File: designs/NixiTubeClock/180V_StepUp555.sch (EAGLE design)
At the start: 8 parts, among them IC1 LM555D, IC2 IRF740SPBF, T1 BC547

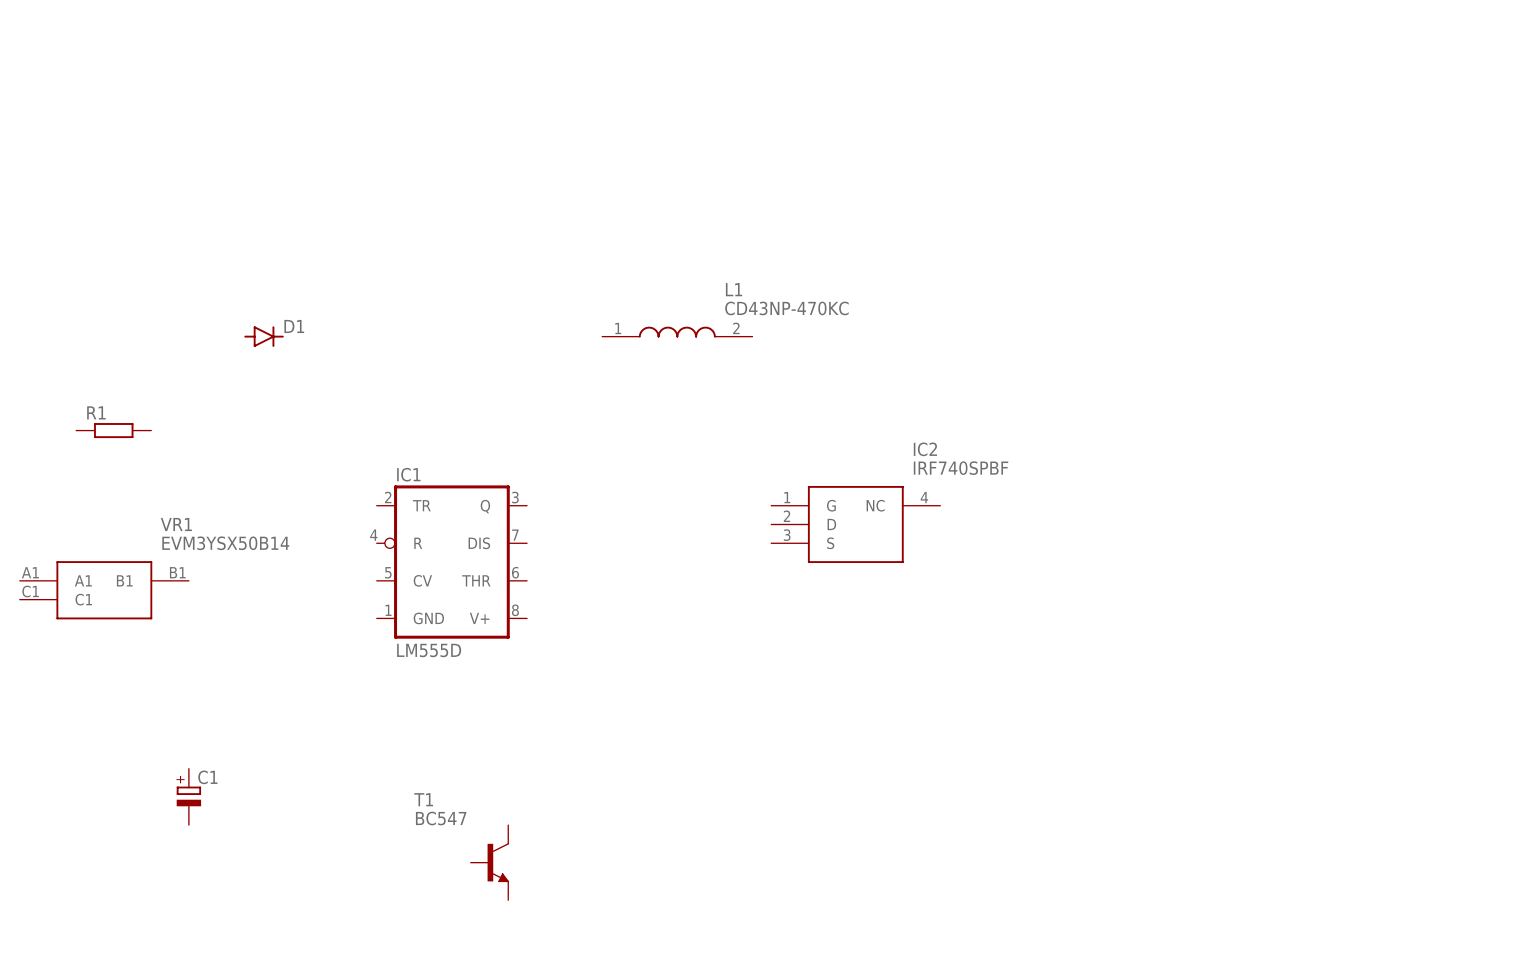
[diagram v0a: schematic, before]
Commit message: added first IN-4 Design and edited mainboard to fit all screws for IN-4
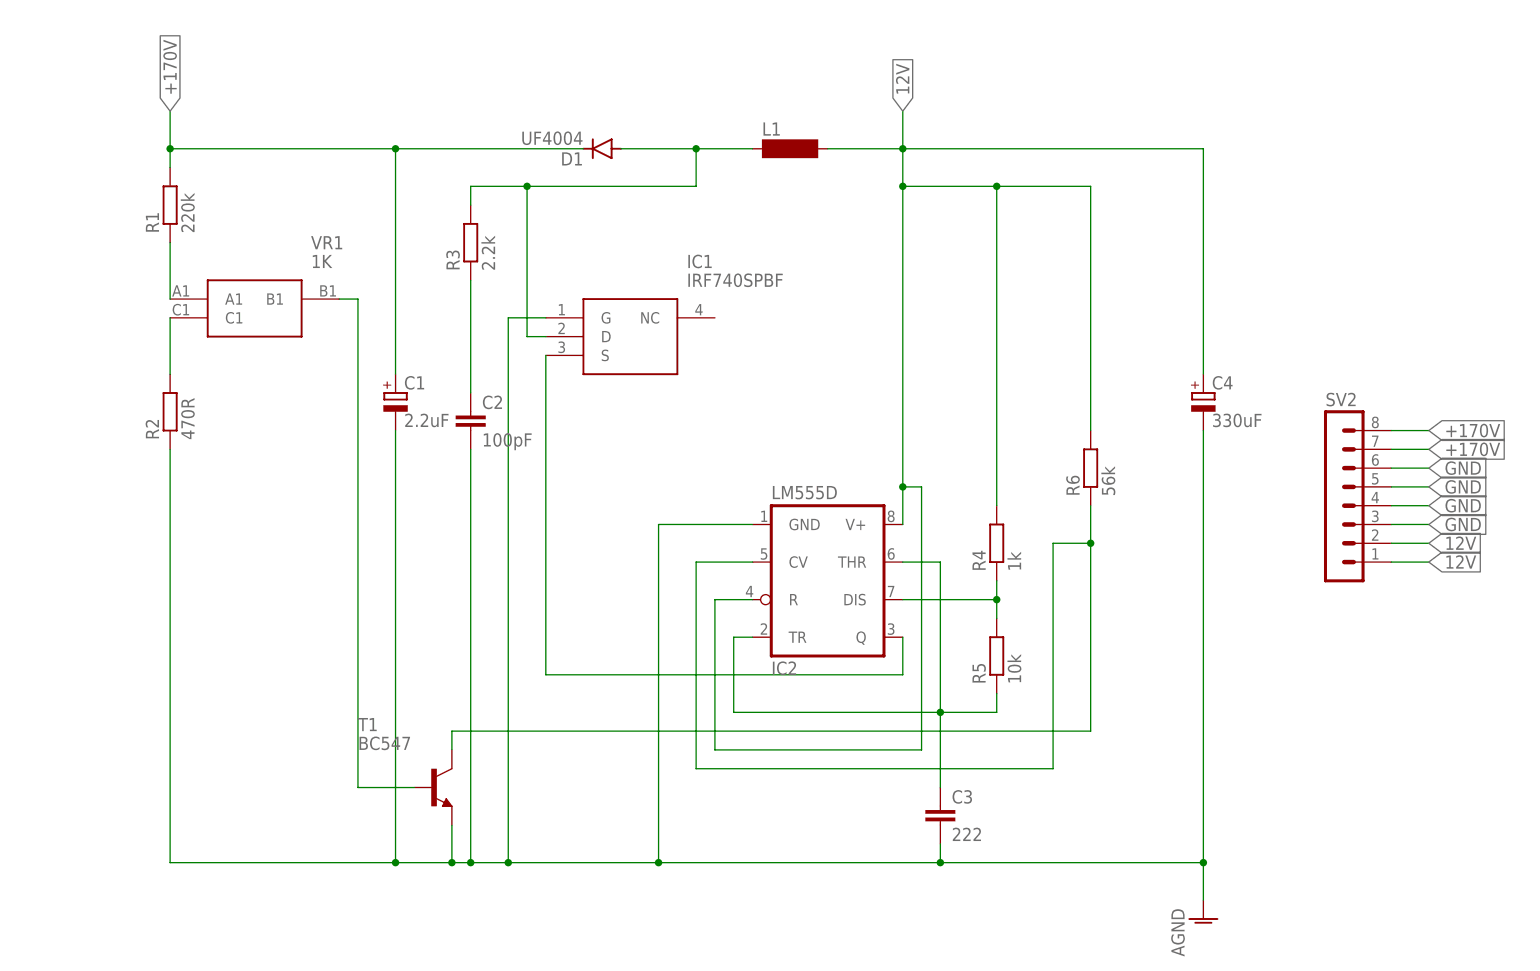
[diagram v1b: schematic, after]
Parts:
- added C2: 100pF, rcl:C-EU050-024X044
- added C3: 222, rcl:C-EU050-024X044
- added C4: 330uF, rcl:CPOL-EUE2.5-6
- added R2: 470R, CommonParts:CARBON/METAL_FILM_RESISTOR0207/10
- added R3: 2.2k, CommonParts:CARBON/METAL_FILM_RESISTOR0207/10
- added R4: 1k, CommonParts:CARBON/METAL_FILM_RESISTOR0207/10
- added R5: 10k, CommonParts:CARBON/METAL_FILM_RESISTOR0207/10
- added R6: 56k, CommonParts:CARBON/METAL_FILM_RESISTOR0207/10
- added SV2: (no value), con-lstb:MA08-1
- C1: value (none) -> 2.2uF
- D1: value (none) -> UF4004
- IC1: value LM555D -> IRF740SPBF; device linear:LM555D -> CommonParts:IRF740SPBF
- IC2: value IRF740SPBF -> LM555D; device CommonParts:IRF740SPBF -> linear:LM555D
- L1: value CD43NP-470KC -> (none); device CommonParts:CD43NP-470KC -> inductor-neosid:SD12K100
- R1: value (none) -> 220k
- VR1: value EVM3YSX50B14 -> 1K
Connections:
- new net +170V: C1.+, D1.C, R1.2, SV2.7, SV2.8
- new net 12V: C4.+, IC2.R, IC2.V+, L1.2, R4.2, R6.2, SV2.1, SV2.2
- new net GND: C1.-, C2.2, C3.2, C4.-, IC1.G, IC2.GND, R2.1, SV2.3, SV2.4, SV2.5, SV2.6, T1.E
- new net N$1: R2.2, VR1.C1
- new net N$10: IC2.DIS, R4.1, R5.2
- new net N$12: IC1.S, IC2.Q
- new net N$2: R1.1, VR1.A1
- new net N$4: T1.B, VR1.B1
- new net N$5: D1.A, IC1.D, L1.1, R3.2
- new net N$7: IC2.CV, R6.1, T1.C
- new net N$8: C2.1, R3.1
- new net N$9: C3.1, IC2.THR, IC2.TR, R5.1
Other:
- moved on the sheet: C1, D1, R1, T1, VR1

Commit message: modified nixi proj. and added EasterRadio project
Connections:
- net GND: now also IC1.S; no longer IC1.G
- net N$12: now also IC1.G; no longer IC1.S
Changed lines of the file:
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@@
 <pinref part="IC2" gate="A" pin="Q"/>
 <wire x1="116.84" y1="45.72" x2="116.84" y2="40.64" width="0.1524" layer="91"/>
-<wire x1="116.84" y1="40.64" x2="68.58" y2="40.64" width="0.1524" layer="91"/>
-<pinref part="IC1" gate="G$1" pin="S"/>
-<wire x1="68.58" y1="83.82" x2="68.58" y2="40.64" width="0.1524" layer="91"/>
+<wire x1="116.84" y1="40.64" x2="63.5" y2="40.64" width="0.1524" layer="91"/>
+<pinref part="IC1" gate="G$1" pin="G"/>
+<wire x1="68.58" y1="88.9" x2="63.5" y2="88.9" width="0.1524" layer="91"/>
+<wire x1="63.5" y1="88.9" x2="63.5" y2="40.64" width="0.1524" layer="91"/>
 </segment>
 </net>
@@
 <wire x1="48.26" y1="15.24" x2="55.88" y2="15.24" width="0.1524" layer="91"/>
 <wire x1="55.88" y1="15.24" x2="55.88" y2="20.32" width="0.1524" layer="91"/>
-<pinref part="IC1" gate="G$1" pin="G"/>
-<wire x1="68.58" y1="88.9" x2="63.5" y2="88.9" width="0.1524" layer="91"/>
 <wire x1="55.88" y1="15.24" x2="58.42" y2="15.24" width="0.1524" layer="91"/>
-<wire x1="58.42" y1="15.24" x2="63.5" y2="15.24" width="0.1524" layer="91"/>
-<wire x1="63.5" y1="15.24" x2="63.5" y2="88.9" width="0.1524" layer="91"/>
 <junction x="55.88" y="15.24"/>
 <pinref part="C1" gate="G$1" pin="-"/>
@@
 <wire x1="96.52" y1="60.96" x2="83.82" y2="60.96" width="0.1524" layer="91"/>
 <wire x1="83.82" y1="60.96" x2="83.82" y2="15.24" width="0.1524" layer="91"/>
-<wire x1="83.82" y1="15.24" x2="63.5" y2="15.24" width="0.1524" layer="91"/>
-<junction x="63.5" y="15.24"/>
+<wire x1="83.82" y1="15.24" x2="68.58" y2="15.24" width="0.1524" layer="91"/>
 <pinref part="C4" gate="G$1" pin="-"/>
+<wire x1="68.58" y1="15.24" x2="58.42" y2="15.24" width="0.1524" layer="91"/>
 <wire x1="157.48" y1="73.66" x2="157.48" y2="15.24" width="0.1524" layer="91"/>
 <wire x1="157.48" y1="15.24" x2="121.92" y2="15.24" width="0.1524" layer="91"/>
@@
 <wire x1="157.48" y1="10.16" x2="157.48" y2="15.24" width="0.1524" layer="91"/>
 <junction x="157.48" y="15.24"/>
+<pinref part="IC1" gate="G$1" pin="S"/>
+<wire x1="68.58" y1="83.82" x2="68.58" y2="15.24" width="0.1524" layer="91"/>
+<junction x="68.58" y="15.24"/>
 </segment>
 </net>
